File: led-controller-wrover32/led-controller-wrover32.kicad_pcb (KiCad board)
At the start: 2 copper layers, 36 x 36 mm, 43 parts, among them J1 Micro_SD_Card, J2 Conn_01x12, J3 USB_B_Micro, J4 Conn_01x12, J5 Conn_01x04 DNS, J6 Conn_01x02 DNS, J7 Conn_01x02 DNS, J8 Conn_01x05, Q1 MMBT2222A-TP, Q2 MMBT2222A-TP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

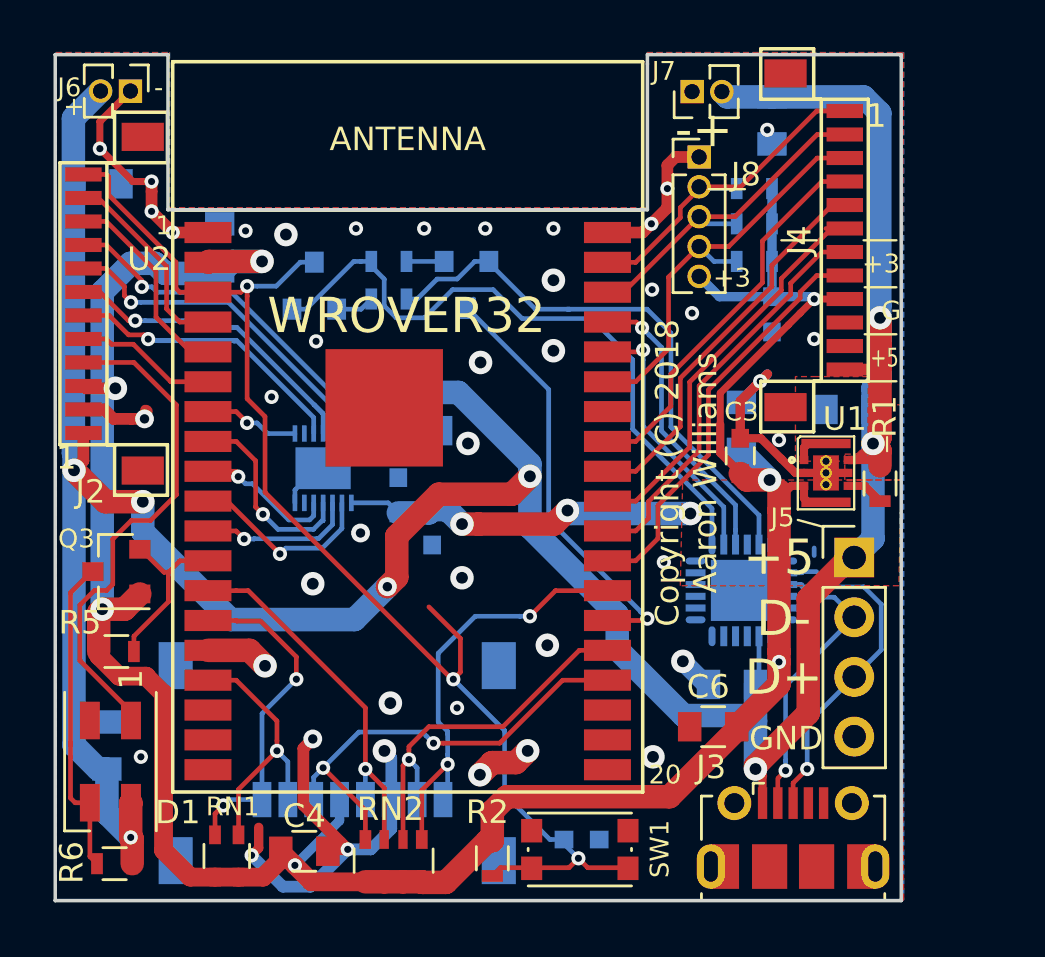
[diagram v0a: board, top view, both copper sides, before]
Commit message: Fixed some silkscreen issues.
Signed-off-by: Aaron Williams <aaron.w2@gmail.com>
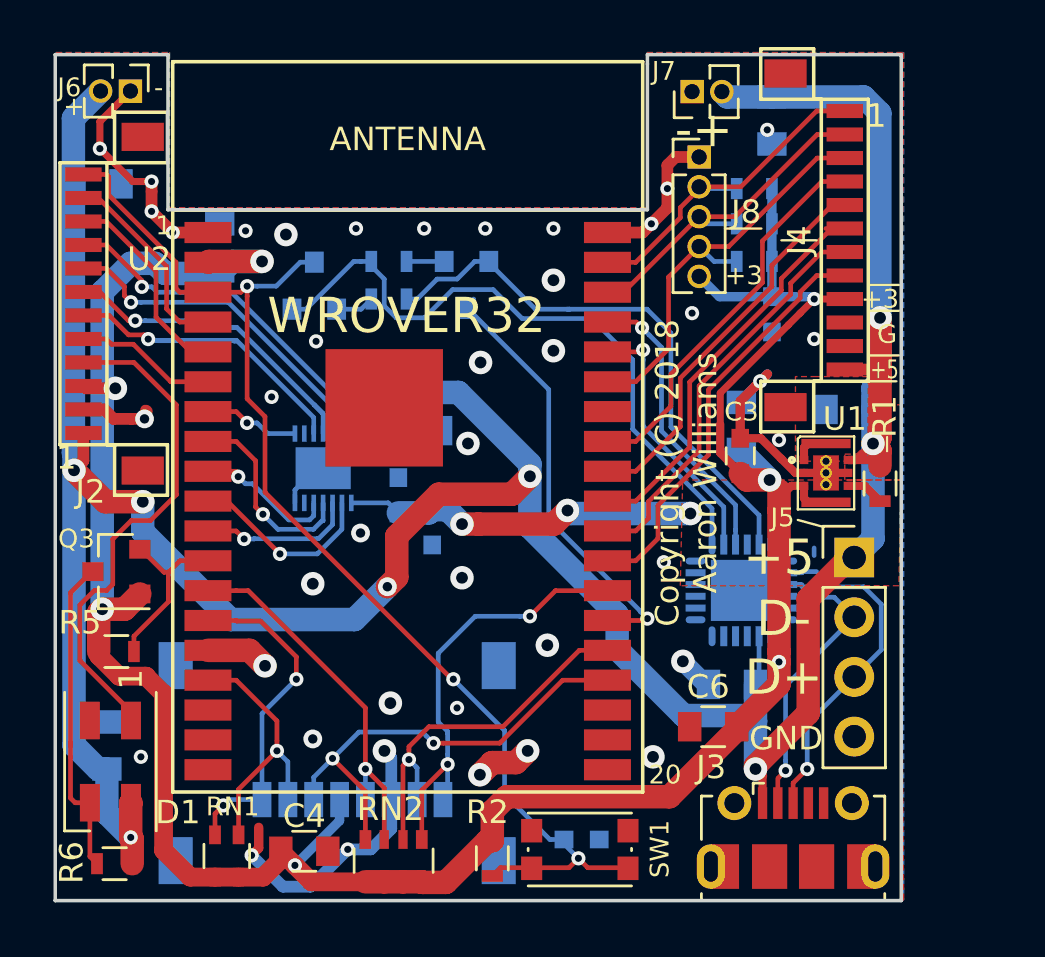
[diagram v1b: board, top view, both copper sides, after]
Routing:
- net GND: track 60.5 -> 53.2 mm, vias 42 -> 41
- net /RESET: track 54.0 -> 50.3 mm

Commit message: Fixed several issues.
1. GPIOs 16 and 17 should not be connected.
2. GPIO 35 was mislabeled GPIO36.  It's input only and would not have
   been able to drive the TS pin oin the MAX chip.
3. Routed GPIO35 to J4.
4. Added a 0.1uF bypass capacitor for Wrover32 like the datasheet recommends.
5. Added another 3.3v pin to J4 after removing GPIOs 16 and 17.

Signed-off-by: Aaron Williams <aaron.w2@gmail.com>
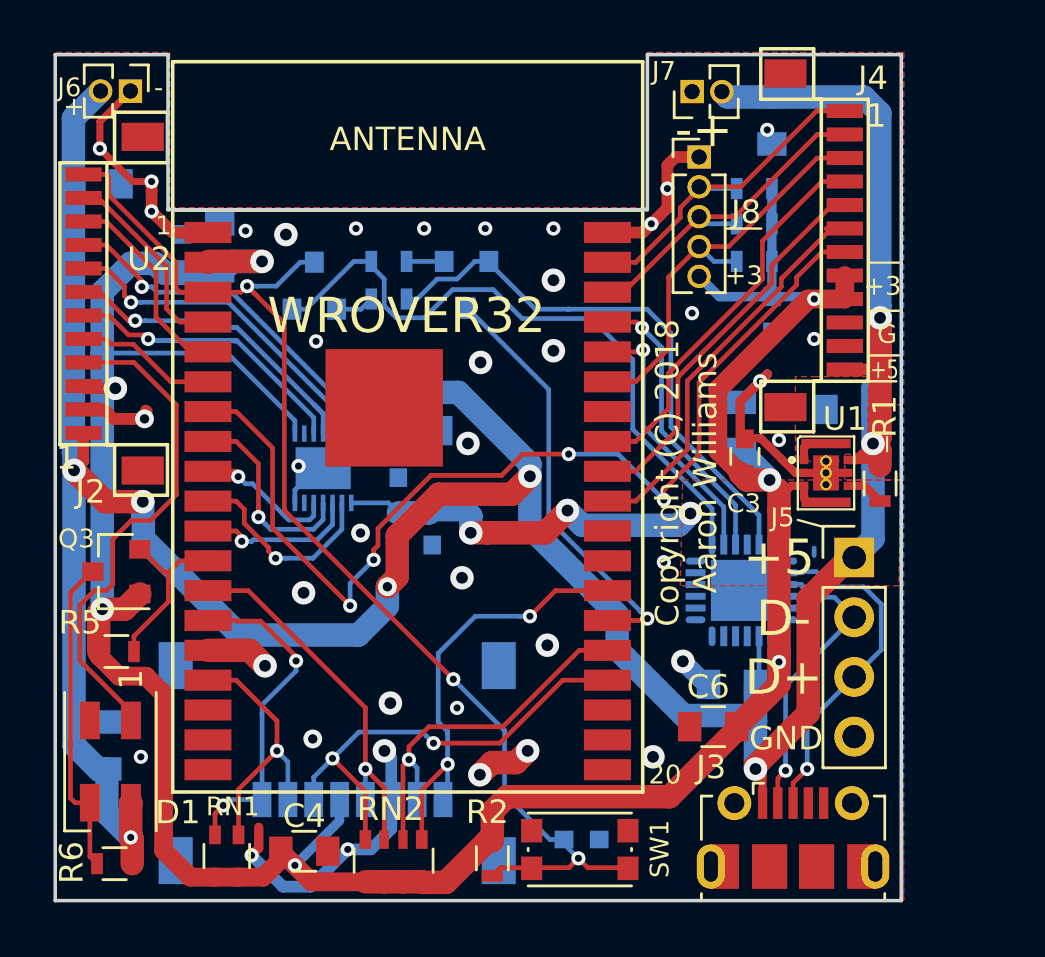
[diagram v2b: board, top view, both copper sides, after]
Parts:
- added C16: 1uF 10V, Capacitors_SMD:C_0603, B.Cu at (55.4, 50.4)
- moved C3 0.20 mm to (79.3, 59.1)
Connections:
- J4 pad 7: /IO17 -> /IO35
- J4 pad 8: /IO16 -> +3V3
- U2 pad 27: /IO16 -> Net-(U2-Pad27)
- U2 pad 28: /IO17 -> Net-(U2-Pad28)
- U2 pad 7: /IO36 -> /IO35
- U4 pad 8: /IO36 -> +3V3
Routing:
- net /IO35: track 0.00 -> 43.9 mm, vias 0 -> 4
- net +3V3: track 129.1 -> 161.6 mm
- net /IO16: track 17.7 -> 0.00 mm
- net /IO17: track 17.3 -> 0.00 mm
- net /IO36: track 4.10 -> 0.00 mm, vias 1 -> 0
- net VBUS: track 146.0 -> 147.2 mm
- net /IO25: track 8.19 -> 8.78 mm
- net GND: vias 41 -> 40
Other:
- board text added: "Rev 1.3"
- board text removed: "Rev 1.2"

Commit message: Added microphone and updated README
Signed-off-by: Aaron Williams <aaron.w2@gmail.com>
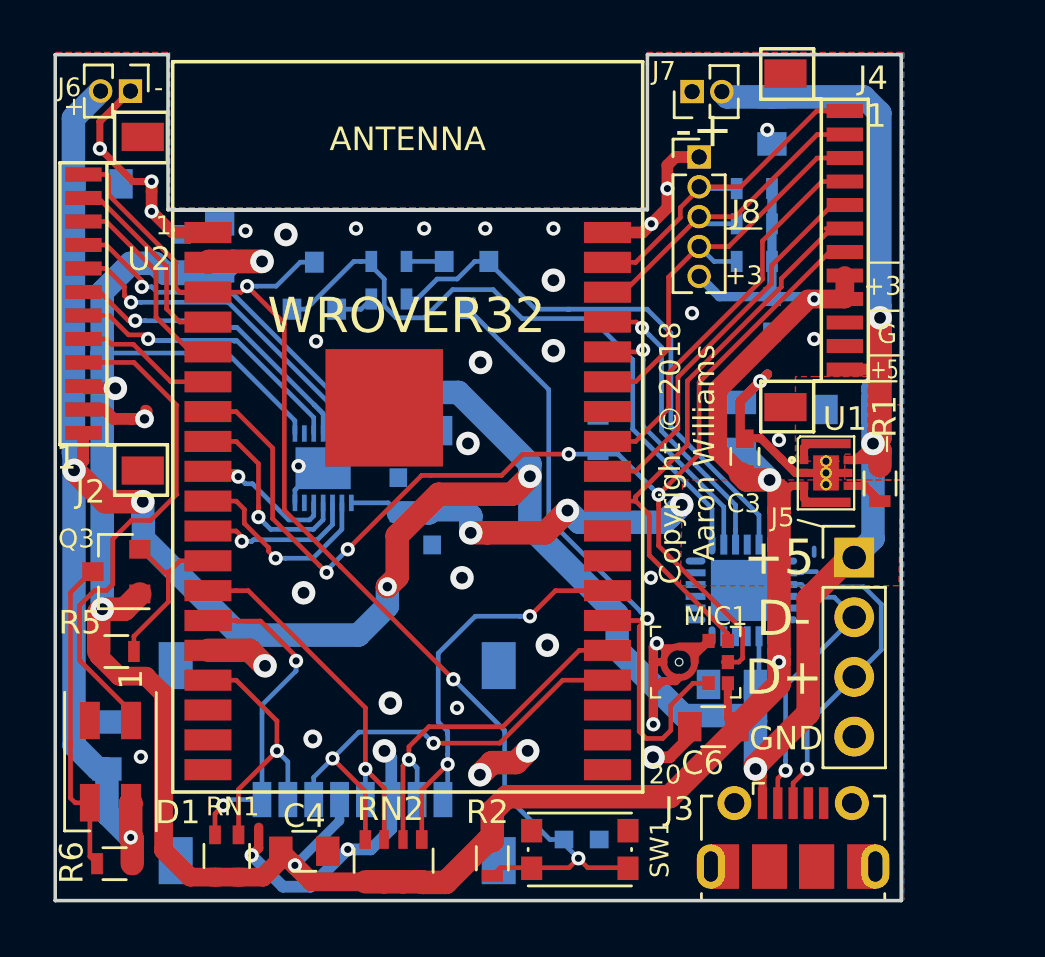
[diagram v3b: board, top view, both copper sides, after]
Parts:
- added MIC1: SPH0645LM4H-B, digikey-footprints:SPH0645LM4H-B, F.Cu at (76.5, 67.8)
- added R10: 100K, Resistors_SMD:R_0603, B.Cu at (73.1, 58.2)
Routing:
- net GND: track 53.2 -> 65.1 mm
- net /GPIO0: track 18.4 -> 27.8 mm
- net /IO5: track 17.4 -> 25.0 mm
- net /IO35: track 43.9 -> 50.2 mm
- net +3V3: track 161.6 -> 163.3 mm
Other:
- board text added: "Copyright © 2018 Aaron Williams"
- board text added: "Rev 1.4"
- board text removed: "Copyright (C) 2018 Aaron Williams"
- board text removed: "Rev 1.3"

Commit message: Changed the connectors from JST to a TE 1-1734595-2 connector.
This connector uses crimped on pins, but it may be easier to deal
with since it works with 28 gauge wire whereas the JST requires 30
gauge (though I ordered some 28AWG that should fit it).

This can always be reverted.

Signed-off-by: Aaron Williams <aaron.w2@gmail.com>
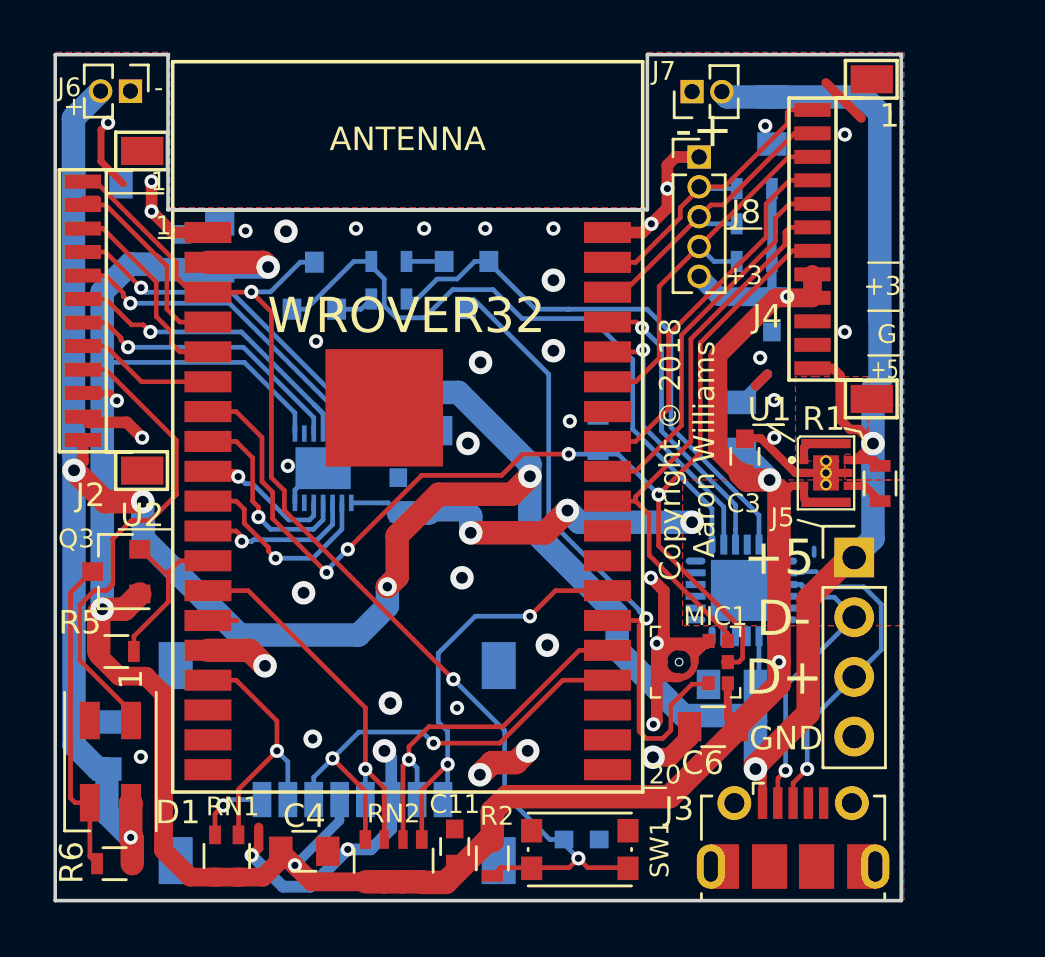
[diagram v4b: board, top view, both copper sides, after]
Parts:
- removed C1: 10uF 10V, Capacitors_SMD:C_0805
- C11: moved to F.Cu
- J2, J4: footprint aaron:BM12B-SRSS-TB -> aaron:TE_1_1734595_2_12Pos_1.0mm_Vert_SMD
- moved C11 13.6 mm to (67.0, 75.7), turned to 90 degrees
- moved J4 1.38 mm to (82.2, 49.9), turned to 90 degrees
- moved J2 0.30 mm to (51.2, 52.9)
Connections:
- J2 pad 1: VBUS -> /RESET
- J2 pad 10: /SENSOR_VN -> +3V3
- J2 pad 11: /SENSOR_VP -> GND
- J2 pad 12: /RESET -> VBUS
- J2 pad 2: GND -> /SENSOR_VP
- J2 pad 3: +3V3 -> /SENSOR_VN
- J2 pad 4: /DO -> /IO25_H
- J2 pad 5: /IO34 -> /IO26_H
- J2 pad 6: /IO33_H -> /IO32_H
- J2 pad 7: /IO32_H -> /IO33_H
- J2 pad 8: /IO26_H -> /IO34
- J2 pad 9: /IO25_H -> /DO
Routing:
- net +3V3: track 163.3 -> 152.3 mm
- net /IO12: track 14.1 -> 4.38 mm, vias 2 -> 1
- net /IO33_H: track 16.1 -> 12.3 mm
- net VBUS: track 147.2 -> 143.7 mm, vias 8 -> 7
- net /IO21: track 17.5 -> 16.3 mm
- net /IO22: track 15.1 -> 13.9 mm
- net /RESET: track 50.2 -> 49.1 mm
- net /IO23: track 14.7 -> 13.7 mm
- net /DO: track 21.5 -> 20.5 mm
- net /IO5: track 25.0 -> 24.1 mm
- net /SENSOR_VN: track 9.45 -> 8.66 mm
- net GND: track 65.1 -> 65.8 mm, vias 40 -> 42
- net /SENSOR_VP: track 8.55 -> 9.09 mm
- net /IO19: track 17.2 -> 16.6 mm

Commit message: Finalized v1.4 design.
Added USB protection diodes.
Cleaned up routing some more.
Cleaned up the silk screening after getting connector models.

Signed-off-by: Aaron Williams <aaron.w2@gmail.com>
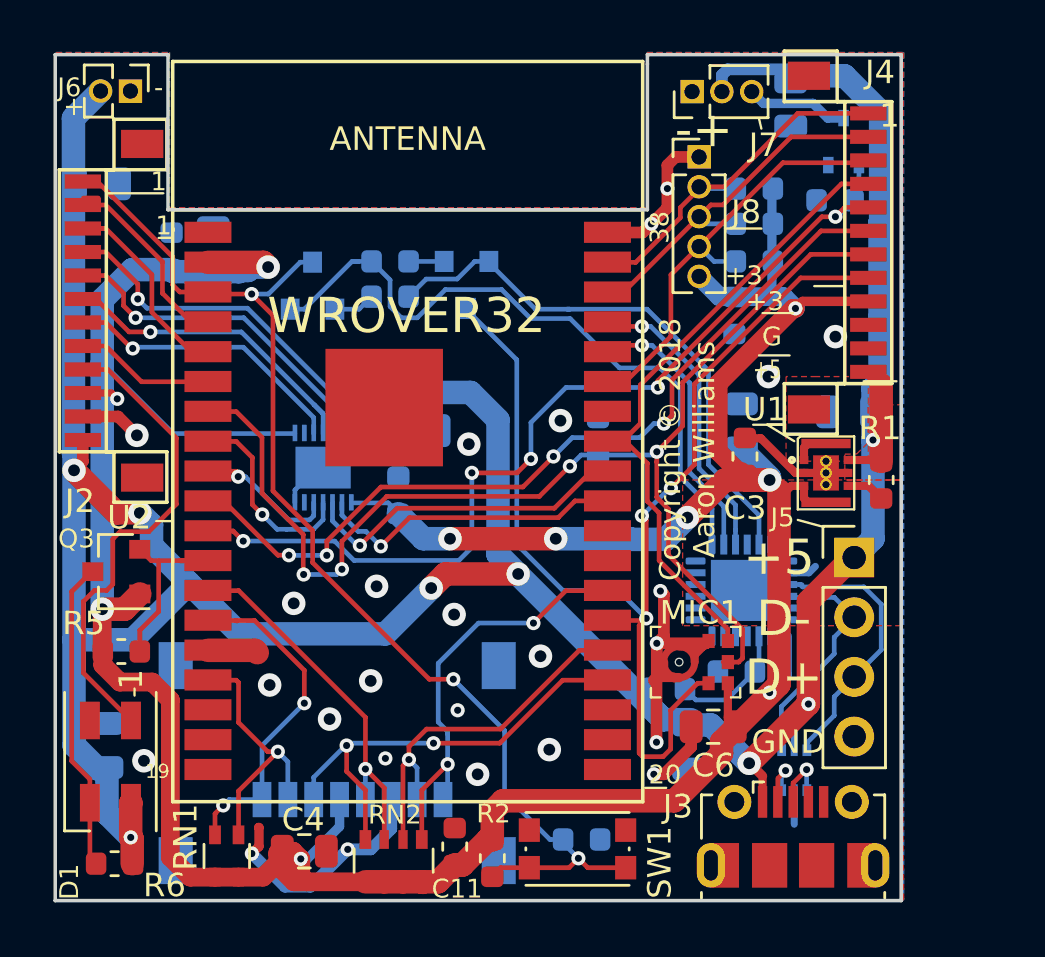
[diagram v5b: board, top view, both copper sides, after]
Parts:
- added C1: 10uF, Capacitor_SMD:C_0805_2012Metric, B.Cu at (83.8, 57.2)
- added D2: USBLC6-2SC6, TO_SOT_Packages_SMD:SOT-666, B.Cu at (81.5, 72.5)
- added Q4: BSS214NW, TO_SOT_Packages_SMD:SOT-323_SC-70, B.Cu at (83.5, 45.7)
- added R11: 1m, Resistor_SMD:R_0603_1608Metric, B.Cu at (83.2, 48.2)
- added R12: 22.1k, Resistor_SMD:R_0603_1608Metric, B.Cu at (76.0, 69.0)
- added R13: 47.5k, Resistor_SMD:R_0603_1608Metric, B.Cu at (79.0, 68.2)
- C10, C12, C13, C14, C2, C4, C6, C7, C9: value 10uF 10V -> 10uF; footprint Capacitors_SMD:C_0805 -> Capacitor_SMD:C_0805_2012Metric
- C11, C15, C16, C3, C8: value 1uF 10V -> 1uF; footprint Capacitors_SMD:C_0603 -> Capacitor_SMD:C_0603_1608Metric
- C5: value 0.1uF 10V -> 0.1uF; footprint Capacitors_SMD:C_0603 -> Capacitor_SMD:C_0603_1608Metric
- J2, J4: footprint aaron:TE_1_1734595_2_12Pos_1.0mm_Vert_SMD -> Connectors_JST-BM12B-SURS-TF:BM12B-SRSS-TB
- J7: value Conn_01x02 DNS -> Conn_01x03; footprint Pin_Headers:Pin_Header_Straight_1x02_Pitch1.27mm -> Pin_Headers:Pin_Header_Straight_1x03_Pitch1.27mm
- R1, R10, R2, R3, R4, R5, R6, R7, R8, R9: footprint Resistors_SMD:R_0603 -> Resistor_SMD:R_0603_1608Metric
- RN1: footprint Resistors_SMD:R_Array_Convex_2x0603 -> Resistor_SMD:R_Array_Convex_2x0603
- RN2: footprint Resistors_SMD:R_Array_Convex_4x0603 -> Resistor_SMD:R_Array_Convex_4x0603
- SW1: footprint aaron:SW_SPST_KMR2 -> Buttons_Switches_SMD:SW_SPST_KMR2
- U3: footprint Maxim:QFN-24-1EP_4x4mm_Pitch0.5mm -> Housings_DFN_QFN:QFN-24-1EP_4x4mm_Pitch0.5mm_rounded_corners
- moved C10 3.24 mm to (77.0, 71.5), turned to 270 degrees
- moved J4 2.38 mm to (84.6, 50.0), turned to 270 degrees
- moved C15 1.60 mm to (78.9, 53.1)
- moved C14 1.06 mm to (81.3, 44.1)
- moved J3 0.94 mm to (81.4, 75.3)
- moved C16 0.45 mm to (55.0, 50.4)
- moved C12 0.29 mm to (56.7, 50.3)
- moved R5 0.21 mm to (52.8, 67.4)
- moved R1 0.16 mm to (85.2, 60.1)
- moved R4 0.11 mm to (64.2, 52.3)
- moved SW1 0.10 mm to (72.2, 75.8)
- moved Q2 0.08 mm to (61.0, 51.8)
- turned U4 to 90 degrees
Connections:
- J2 pad 1: /RESET -> VBUS
- J2 pad 10: +3V3 -> /SENSOR_VN
- J2 pad 11: GND -> /SENSOR_VP
- J2 pad 12: VBUS -> /RESET
- J2 pad 2: /SENSOR_VP -> GND
- J2 pad 3: /SENSOR_VN -> +3V3
- J2 pad 4: /IO25_H -> /DO
- J2 pad 5: /IO26_H -> /IO34
- J2 pad 6: /IO32_H -> /IO33_H
- J2 pad 7: /IO33_H -> /IO32_H
- J2 pad 8: /IO34 -> /IO18_H
- J2 pad 9: /DO -> /IO5_H
- J3 pad 2: /USB_D- -> Net-(D2-Pad3)
- J3 pad 3: /USB_D+ -> Net-(D2-Pad1)
- J4 pad 5: /IO18 -> /IO26
- J4 pad 6: /IO5 -> /IO25
- J4 pad 8: +3V3 -> /IO0
- MIC1 pad 1: /IO5 -> /IO19
- MIC1 pad 4: /GPIO0 -> /IO0
- Q1 pad 3: /GPIO0 -> /IO0
- U2 pad 25: /GPIO0 -> /IO0
- U3 pad 8: VBUS -> Net-(R12-Pad2)
- U4 pad 12: /IO26_H -> /IO18_H
- U4 pad 13: /IO25_H -> /IO5_H
- U4 pad 2: /IO25 -> /IO5
- U4 pad 3: /IO26 -> /IO18
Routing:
- net /IO0: track 0.00 -> 50.8 mm, vias 0 -> 3
- net /IO26: track 6.82 -> 40.8 mm, vias 1 -> 5
- net /GPIO0: track 27.7 -> 0.00 mm, vias 1 -> 0
- net /IO25: track 8.78 -> 35.9 mm, vias 1 -> 4
- net GND: track 65.8 -> 49.9 mm, vias 42 -> 25
- net /IO5_H: track 0.00 -> 15.4 mm, vias 0 -> 1
- net /IO25_H: track 15.0 -> 0.00 mm, vias 1 -> 0
- net /IO26_H: track 14.5 -> 0.00 mm, vias 1 -> 0
- net /IO18_H: track 0.00 -> 14.0 mm, vias 0 -> 1
- net /IO5: track 24.1 -> 13.2 mm, vias 0 -> 1
- net /IO19: track 16.6 -> 27.0 mm
- net /IO12: track 4.38 -> 14.4 mm, vias 1 -> 2
- net +3V3: track 152.3 -> 159.5 mm
- net Net-(R12-Pad2): track 0.00 -> 5.24 mm
- net /FET_1A: track 0.00 -> 4.33 mm
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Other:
- board text added: "19"
- board text added: "38"
